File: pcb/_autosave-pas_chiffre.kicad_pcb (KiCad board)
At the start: 2 copper layers, 96.3 x 87.5 mm, 26 parts, among them J1 Conn_01x06_Pin, J2 Conn_01x06_Pin, SW1 SW_SPST, SW10 SW_SPST, SW11 SW_SPST, SW12 SW_SPST, SW13 SW_SPST, SW14 SW_SPST, SW15 SW_SPST, SW16 SW_SPST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

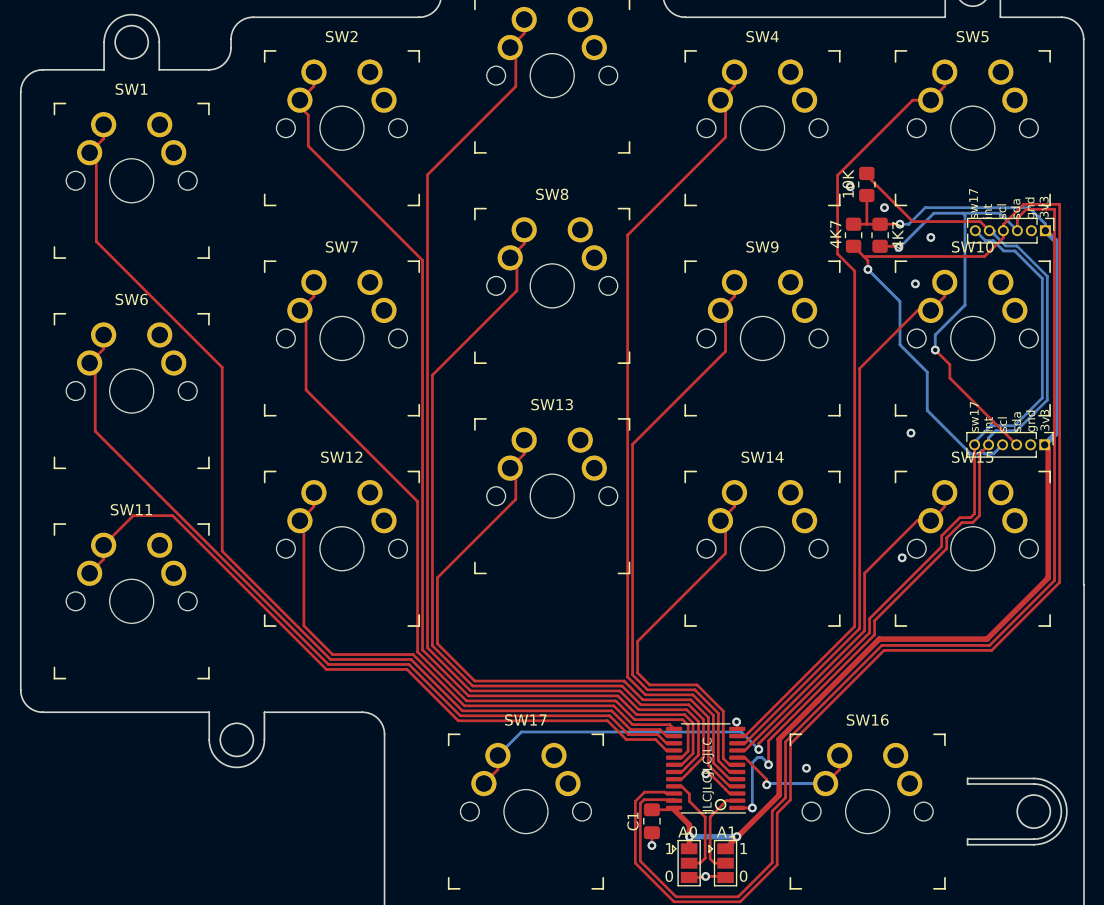
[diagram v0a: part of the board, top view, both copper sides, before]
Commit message: fixed switch footprint
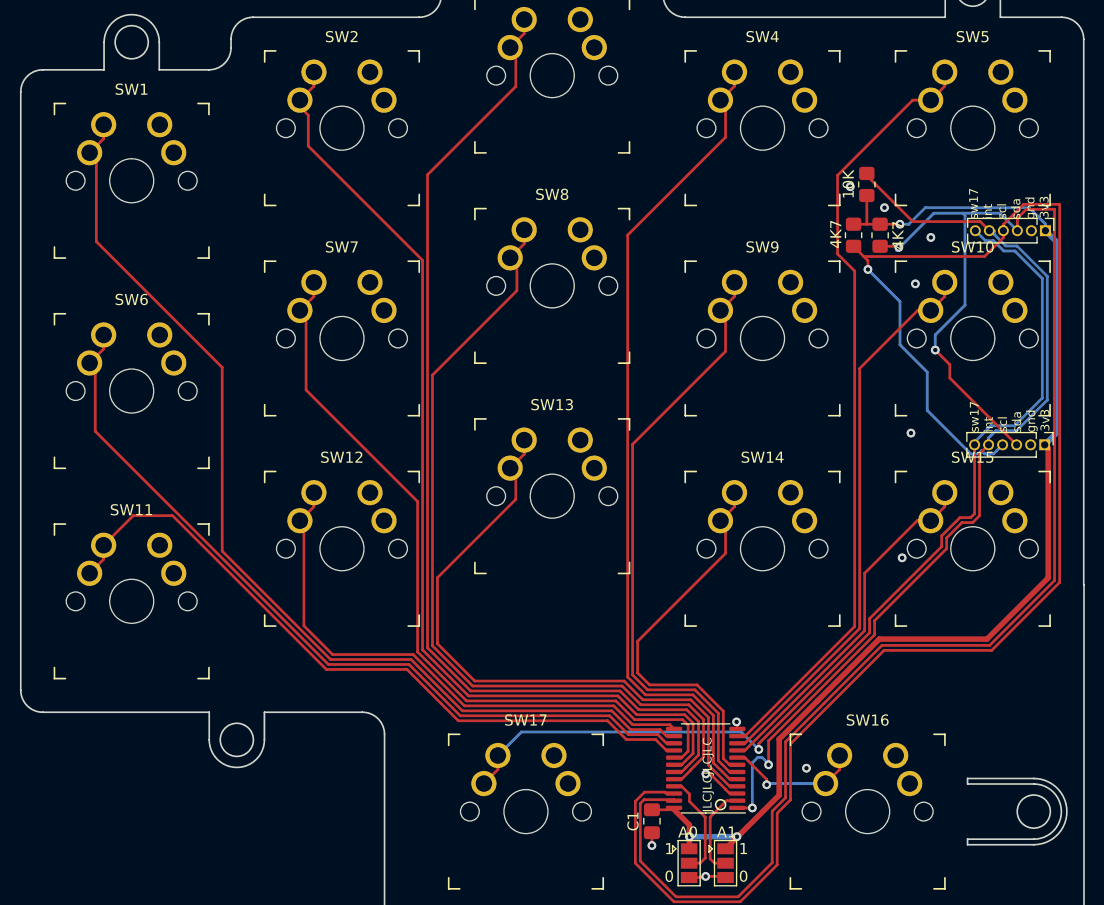
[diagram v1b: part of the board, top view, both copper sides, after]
